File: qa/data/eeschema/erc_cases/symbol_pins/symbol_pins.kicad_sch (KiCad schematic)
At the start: 1 part, among them U1 Q

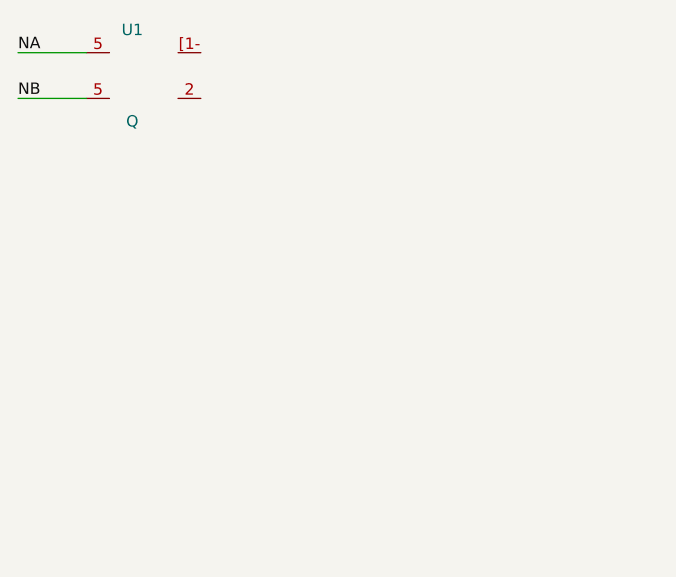
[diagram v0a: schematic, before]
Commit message: qa: extend four ERC fixtures to reach what the S2-4b-7/8 sweep found unpinned
similar_labels gains a subsheet with a local daTa (case variants on two sheets are fine),
similar_power an ordinary part valued gnd (only power pins compare), symbol_pins a twin
whose duplicate pin numbers are jumpers, footprints a unit with no footprint and a
Resistor_SMD:R_* filter (a ':' filter matches the whole id). kicad-cli regenerated
every report; all match.

Co-Authored-By: Claude Opus 5.5 (1M context) <noreply@anthropic.com>
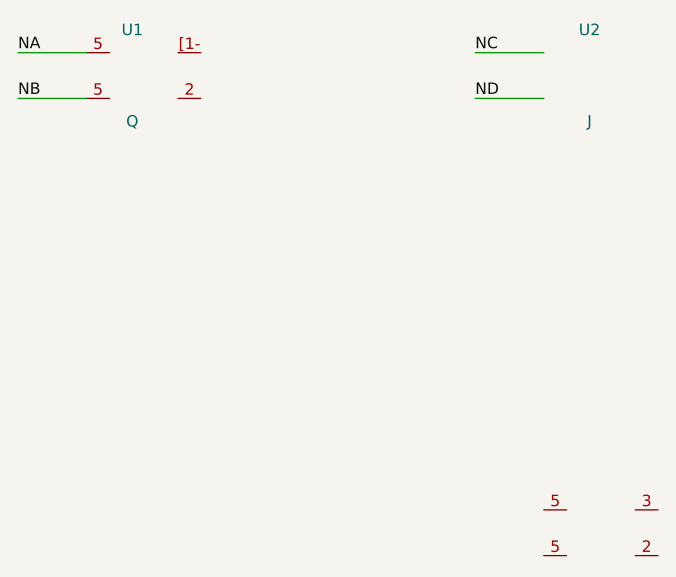
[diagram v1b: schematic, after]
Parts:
- added U2: J, symbol erc:J
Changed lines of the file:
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@@
 	(wire (pts (xy 96.52 104.14) (xy 88.9 104.14)) (stroke (width 0) (type default)))
 	(label "NB" (at 88.9 104.14 0) (effects (font (size 1.27 1.27)) (justify left bottom)))
+	(symbol (lib_id "erc:J") (at 152.4 152.4 0) (unit 1) (body_style 1) (exclude_from_sim no) (in_bom yes) (on_board yes) (dnp no)
+		(property "Reference" "U2" (at 152.4 96.52 0) (effects (font (size 1.27 1.27))))
+		(property "Value" "J" (at 152.4 106.68 0) (effects (font (size 1.27 1.27))))
+		(property "Footprint" "" (at 152.4 152.4 0) (hide yes) (effects (font (size 1.27 1.27))))
+		(property "Datasheet" "" (at 152.4 152.4 0) (hide yes) (effects (font (size 1.27 1.27))))
+		(property "MPN" "X1" (at 152.4 109.22 0) (hide yes) (effects (font (size 1.27 1.27))))
+		(pin "5")
+		(pin "5")
+		(pin "3")
+		(pin "2")
+		(instances (project "symbol_pins" (path "/51111111-2222-3333-4444-555555555555" (reference "U2") (unit 1))))
+	)
+	(wire (pts (xy 147.32 99.06) (xy 139.7 99.06)) (stroke (width 0) (type default)))
+	(label "NC" (at 139.7 99.06 0) (effects (font (size 1.27 1.27)) (justify left bottom)))
+	(wire (pts (xy 147.32 104.14) (xy 139.7 104.14)) (stroke (width 0) (type default)))
+	(label "ND" (at 139.7 104.14 0) (effects (font (size 1.27 1.27)) (justify left bottom)))
 	(sheet_instances (path "/" (page "1")))
 )
